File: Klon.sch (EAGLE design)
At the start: 72 parts, among them IC1 TL072P, IC2 TL072P, IC3 MAX1044

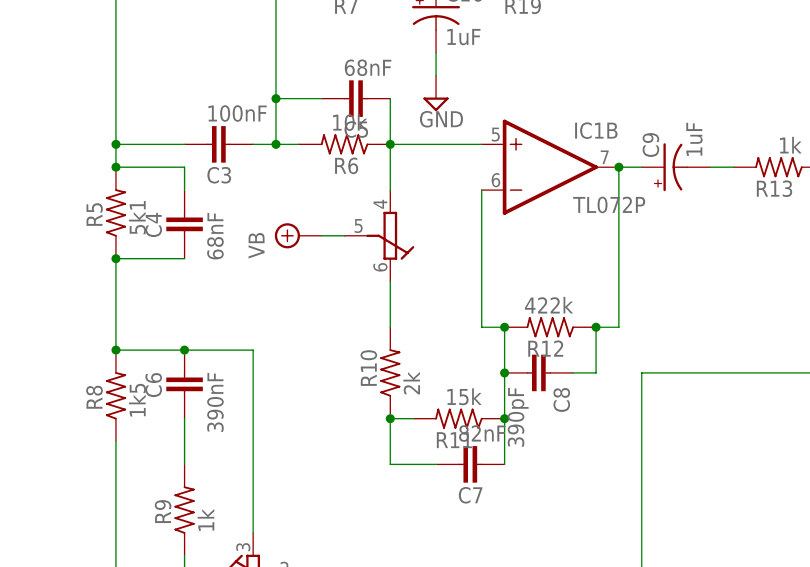
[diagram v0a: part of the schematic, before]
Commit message: Files to Seeed Studio for v1.0
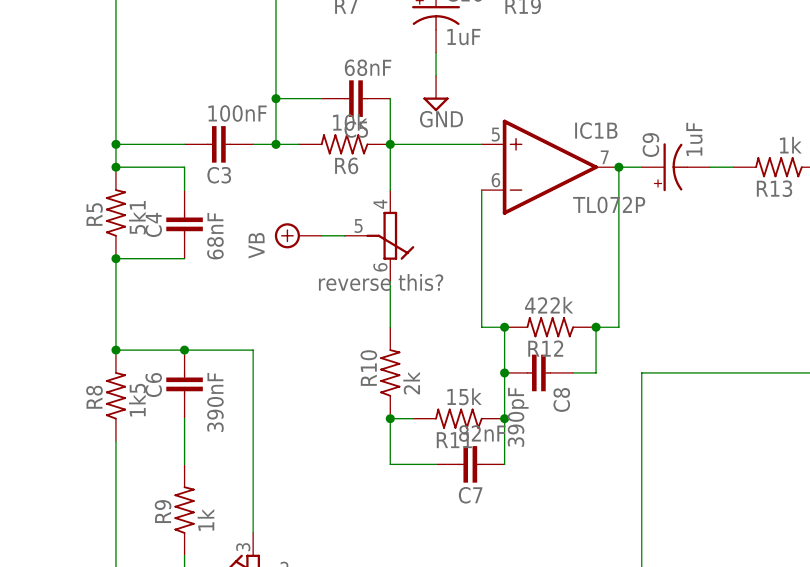
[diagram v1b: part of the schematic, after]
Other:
- note added: "reverse this?"
